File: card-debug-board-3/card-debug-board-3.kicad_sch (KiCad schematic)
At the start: 94 parts, among them J1 USB4105-GF-A, J2 USB4105-GF-A, J3 Conn_01x05, J4 5040501291, J5 2-1734592-0, Q1 PMV450ENEAR, SW1 B3F-1000, SW2 PCM13SMTR, SW3 B3F-1000, SW4 78RB02T, U1 MIC5205-3.3YM5, U2 W25Q16JVSS, U3 RP2040, U4 74AUP1G17, U5 74AUP1G17, U6 IP4234CZ6,125, U7 IP4234CZ6,125, Y1 12 MHz

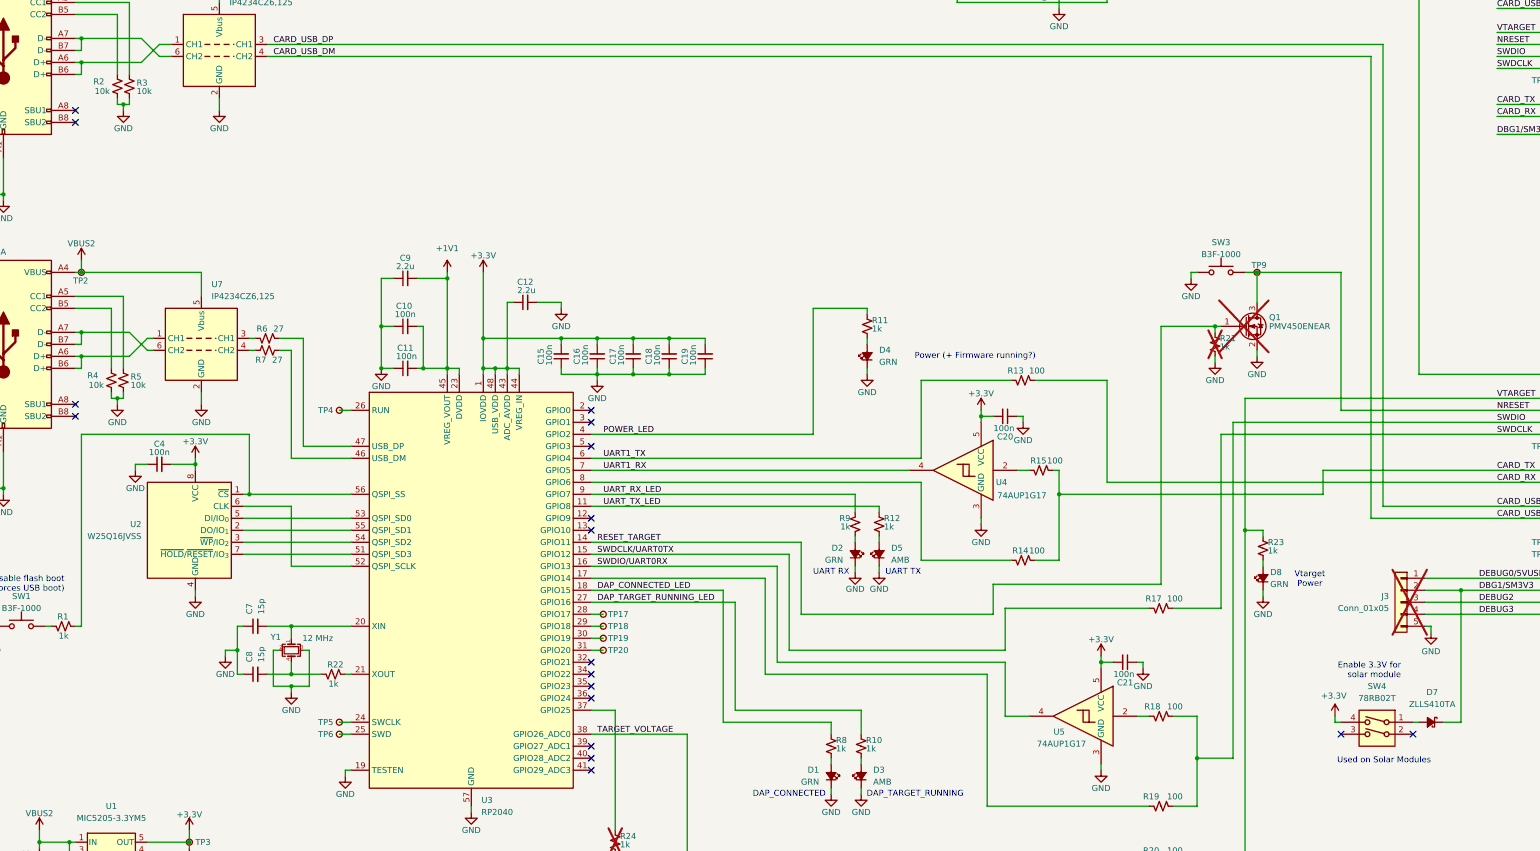
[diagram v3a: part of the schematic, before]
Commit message: Fix labeling of the 3.0 power slide switch which was exactly backwards.
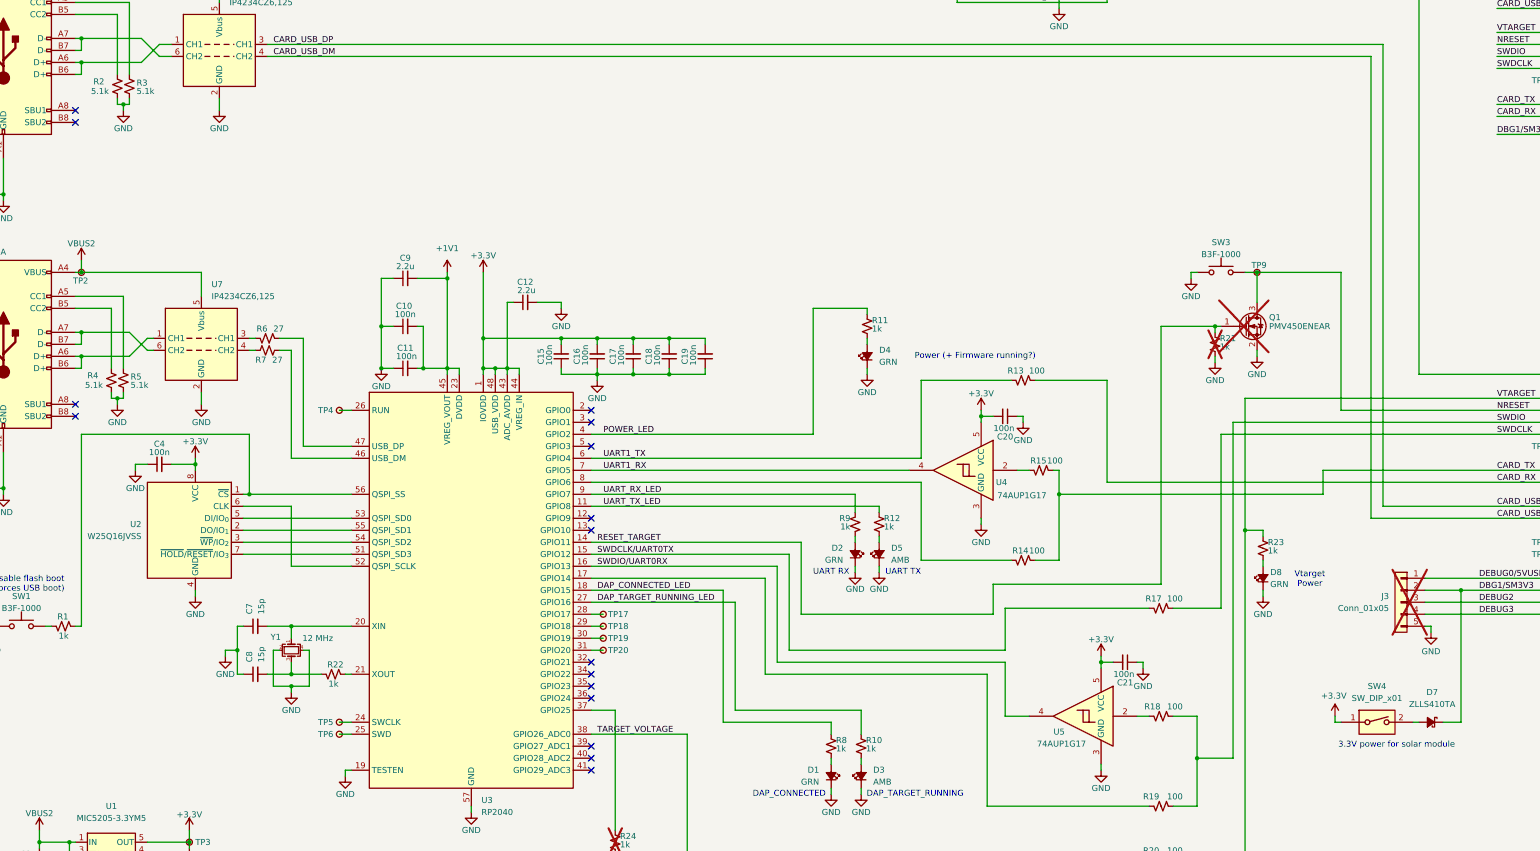
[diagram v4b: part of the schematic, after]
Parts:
- removed SW4: 78RB02T, Button_Switch_THT:SW_DIP_SPSTx02_Slide_6.7x6.64mm_W7.62mm_P2.54mm_LowProfile, symbol Switch:SW_DIP_x02
- added SW4: SW_DIP_x01, Button_Switch_THT:SW_DIP_SPSTx01_Slide_6.7x4.1mm_W7.62mm_P2.54mm_LowProfile, symbol Switch:SW_DIP_x01
- R2, R3, R4, R5: value 10k -> 5.1k; DPN RMCF0603FT10K0CT-ND -> RMCF0603FT5K10CT-ND; MPN RMCF0603FT10K0 -> RMCF0603FT5K10
- Y1: symbol Device:Crystal_GND23_Small -> Device:Crystal_GND24_Small
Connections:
- net +3.3V: now also SW4.1
- net GND: now also Y1.4; no longer Y1.3
- net at C8.2, R22.1: now also Y1.3; no longer Y1.4
- net at D7.2 (A): now also SW4.2
- no-connect marks 18 -> 16
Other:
- note added: "3.3V power for solar module"
- note removed: "Enable 3.3V for solar module"
- note removed: "Used on Solar Modules"
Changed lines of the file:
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@@
 	(title_block
 		(title "Card Debug Board")
-		(date "2025-11-10")
+		(date "2025-11-24")
 		(rev "3.1")
 		(company "Portland State Aerospace Society")
@@
 		)
 	)
-	(text "Enable 3.3V for\nsolar module"
+	(text "3.3V power for solar module"
 		(exclude_from_sim no)
-		(at 331.47 196.596 0)
+		(at 342.9 211.328 0)
 		(effects
 			(font
@@
 		)
 	)
-	(text "Used on Solar Modules"
-		(exclude_from_sim no)
-		(at 337.82 214.63 0)
-		(effects
-			(font
-				(size 1.27 1.27)
-			)
-			(justify right bottom)
-		)
-	)
 	(text "Heartbeat/Misc"
 		(exclude_from_sim no)
@@
 	)
 	(no_connect
-		(at 318.77 208.28)
-	)
-	(no_connect
 		(at 160.02 165.1)
 	)
@@
 	)
 	(no_connect
-		(at 334.01 208.28)
-	)
-	(no_connect
 		(at 160.02 142.24)
 	)
@@
 			)
 		)
-		(property "Value" "10k"
-			(at 54.864 72.136 0)
+		(property "Value" "5.1k"
+			(at 54.102 72.136 0)
 			(effects
 				(font
@@
 			)
 		)
-		(property "Description" "10 kOhms ±1% 0.1W, 1/10W Chip Resistor 0603 (1608 Metric) Automotive AEC-Q200 Thick Film"
+		(property "Description" "5.1 kOhms ±1% 0.1W, 1/10W Chip Resistor 0603 (1608 Metric) Automotive AEC-Q200 Thick Film"
 			(at 59.69 71.12 0)
 			(effects
@@
 			)
 		)
-		(property "DPN" "RMCF0603FT10K0CT-ND"
+		(property "DPN" "RMCF0603FT5K10CT-ND"
 			(at 59.69 71.12 0)
 			(effects
@@
 			)
 		)
-		(property "MPN" "RMCF0603FT10K0"
+		(property "MPN" "RMCF0603FT5K10"
 			(at 59.69 71.12 0)
 			(effects
@@
 			)
 		)
-		(property "Value" "10k"
+		(property "Value" "5.1k"
 			(at 62.484 134.366 0)
 			(effects
@@
 			)
 		)
-		(property "Description" "10 kOhms ±1% 0.1W, 1/10W Chip Resistor 0603 (1608 Metric) Automotive AEC-Q200 Thick Film"
+		(property "Description" "5.1 kOhms ±1% 0.1W, 1/10W Chip Resistor 0603 (1608 Metric) Automotive AEC-Q200 Thick Film"
 			(at 60.96 133.35 0)
 			(effects
@@
 			)
 		)
-		(property "DPN" "RMCF0603FT10K0CT-ND"
+		(property "DPN" "RMCF0603FT5K10CT-ND"
 			(at 60.96 133.35 0)
 			(effects
@@
 			)
 		)
-		(property "MPN" "RMCF0603FT10K0"
+		(property "MPN" "RMCF0603FT5K10"
 			(at 60.96 133.35 0)
 			(effects
@@
 	)
 	(symbol
-		(lib_id "Switch:SW_DIP_x02")
-		(at 326.39 208.28 0)
-		(mirror y)
-		(unit 1)
-		(exclude_from_sim no)
-		(in_bom yes)
-		(on_board yes)
-		(dnp no)
-		(fields_autoplaced yes)
-		(property "Reference" "SW4"
-			(at 326.39 198.12 0)
-			(effects
-				(font
-					(size 1.27 1.27)
-				)
-			)
-		)
-		(property "Value" "78RB02T"
-			(at 326.39 200.66 0)
-			(effects
-				(font
-					(size 1.27 1.27)
-				)
-			)
-		)
-		(property "Footprint" "Button_Switch_THT:SW_DIP_SPSTx02_Slide_6.7x6.64mm_W7.62mm_P2.54mm_LowProfile"
-			(at 326.39 208.28 0)
-			(effects
-				(font
-					(size 1.27 1.27)
-				)
-				(hide yes)
-			)
-		)
-		(property "Datasheet" "https://app-grayhill-website-cms-prod-001.azurewebsites.net/media/4nooheqb/78b-datasheet.pdf"
-			(at 326.39 208.28 0)
-			(effects
-				(font
-					(size 1.27 1.27)
-				)
-				(hide yes)
-			)
-		)
-		(property "Description" "Dip Switch SPST 2 Position Through Hole Slide (Standard) Actuator 150mA 30VDC"
-			(at 326.39 208.28 0)
-			(effects
-				(font
-					(size 1.27 1.27)
-				)
-				(hide yes)
-			)
-		)
-		(property "MFR" "Grayhill Inc."
-			(at 326.39 208.28 0)
-			(effects
-				(font
-					(size 1.27 1.27)
-				)
-				(hide yes)
-			)
-		)
-		(property "MPN" "78RB02T"
-			(at 326.39 208.28 0)
-			(effects
-				(font
-					(size 1.27 1.27)
-				)
-				(hide yes)
-			)
-		)
-		(property "DIS" "DigiKey"
-			(at 326.39 208.28 0)
-			(effects
-				(font
-					(size 1.27 1.27)
-				)
-				(hide yes)
-			)
-		)
-		(property "DPN" "GH7201-ND"
-			(at 326.39 208.28 0)
-			(effects
-				(font
-					(size 1.27 1.27)
-				)
-				(hide yes)
-			)
-		)
-		(pin "3"
-		)
-		(pin "1"
-		)
-		(pin "2"
-		)
-		(pin "4"
-		)
-		(instances
-			(project ""
-				(path "/6ec99451-f949-47af-a175-ad55f6cf8202"
-					(reference "SW4")
-					(unit 1)
-				)
-			)
-		)
-	)
-	(symbol
 		(lib_id "power:GND")
 		(at 218.44 132.08 0)
@@
 			)
 		)
-		(property "Value" "10k"
+		(property "Value" "5.1k"
 			(at 63.754 72.136 0)
 			(effects
@@
 			)
 		)
-		(property "Description" "10 kOhms ±1% 0.1W, 1/10W Chip Resistor 0603 (1608 Metric) Automotive AEC-Q200 Thick Film"
+		(property "Description" "5.1 kOhms ±1% 0.1W, 1/10W Chip Resistor 0603 (1608 Metric) Automotive AEC-Q200 Thick Film"
 			(at 62.23 71.12 0)
 			(effects
@@
 			)
 		)
-		(property "DPN" "RMCF0603FT10K0CT-ND"
+		(property "DPN" "RMCF0603FT5K10CT-ND"
 			(at 62.23 71.12 0)
 			(effects
@@
 			)
 		)
-		(property "MPN" "RMCF0603FT10K0"
+		(property "MPN" "RMCF0603FT5K10"
 			(at 62.23 71.12 0)
 			(effects
@@
 	)
 	(symbol
+		(lib_id "Switch:SW_DIP_x01")
+		(at 326.39 205.74 0)
+		(unit 1)
+		(exclude_from_sim no)
+		(in_bom yes)
+		(on_board yes)
+		(dnp no)
+		(fields_autoplaced yes)
+		(property "Reference" "SW4"
+			(at 326.39 198.12 0)
+			(effects
+				(font
+					(size 1.27 1.27)
+				)
+			)
+		)
+		(property "Value" "SW_DIP_x01"
+			(at 326.39 200.66 0)
+			(effects
+				(font
+					(size 1.27 1.27)
+				)
+			)
+		)
+		(property "Footprint" "Button_Switch_THT:SW_DIP_SPSTx01_Slide_6.7x4.1mm_W7.62mm_P2.54mm_LowProfile"
+			(at 326.39 205.74 0)
+			(effects
+				(font
+					(size 1.27 1.27)
+				)
+				(hide yes)
+			)
+		)
+		(property "Datasheet" "Dip Switch SPST 1 Position Through Hole Slide (Standard) Actuator 100mA 6VDC"
+			(at 326.39 205.74 0)
+			(effects
+				(font
+					(size 1.27 1.27)
+				)
+				(hide yes)
+			)
+		)
+		(property "Description" "1x DIP Switch, Single Pole Single Throw (SPST) switch, small symbol"
+			(at 326.39 205.74 0)
+			(effects
+				(font
+					(size 1.27 1.27)
+				)
+				(hide yes)
+			)
+		)
+		(property "MFR" "Nidec Components Corporation"
+			(at 326.39 205.74 0)
+			(effects
+				(font
+					(size 1.27 1.27)
+				)
+				(hide yes)
+			)
+		)
+		(property "MPN" "CFS-0100MC"
+			(at 326.39 205.74 0)
+			(effects
+				(font
+					(size 1.27 1.27)
+				)
+				(hide yes)
+			)
+		)
+		(property "DIS" "DigiKey"
+			(at 326.39 205.74 0)
+			(effects
+				(font
+					(size 1.27 1.27)
+				)
+				(hide yes)
+			)
+		)
+		(property "DPN" "563-2016-5-ND"
+			(at 326.39 205.74 0)
+			(effects
+				(font
+					(size 1.27 1.27)
+				)
+				(hide yes)
+			)
+		)
+		(pin "1"
+		)
+		(pin "2"
+		)
+		(instances
+			(project ""
+				(path "/6ec99451-f949-47af-a175-ad55f6cf8202"
+					(reference "SW4")
+					(unit 1)
+				)
+			)
+		)
+	)
+	(symbol
 		(lib_id "power:GND")
 		(at 367.03 189.23 0)
@@
 			)
 		)
-		(property "Value" "10k"
-			(at 53.594 134.366 0)
+		(property "Value" "5.1k"
+			(at 52.832 134.366 0)
 			(effects
 				(font
@@
 			)
 		)
-		(property "Description" "10 kOhms ±1% 0.1W, 1/10W Chip Resistor 0603 (1608 Metric) Automotive AEC-Q200 Thick Film"
+		(property "Description" "5.1 kOhms ±1% 0.1W, 1/10W Chip Resistor 0603 (1608 Metric) Automotive AEC-Q200 Thick Film"
 			(at 58.42 133.35 0)
 			(effects
@@
 			)
 		)
-		(property "DPN" "RMCF0603FT10K0CT-ND"
+		(property "DPN" "RMCF0603FT5K10CT-ND"
 			(at 58.42 133.35 0)
 			(effects
@@
 			)
 		)
-		(property "MPN" "RMCF0603FT10K0"
+		(property "MPN" "RMCF0603FT5K10"
 			(at 58.42 133.35 0)
 			(effects
@@
 	)
 	(symbol
-		(lib_id "Device:Crystal_GND23_Small")
+		(lib_id "Device:Crystal_GND24_Small")
 		(at 96.52 190.5 270)
 		(unit 1)
@@
 			)
 		)
-		(property "Datasheet" "https://www.raltron.com/webproducts/specs/CRYSTAL/RH100-12.000-12-1010-X-TR-NS2.pdf"
+		(property "Datasheet" "~"
 			(at 96.52 190.5 0)
 			(effects
@@
 			)
 		)
-		(property "Description" "12 MHz ±10ppm Crystal 12pF 50 Ohms 4-SMD, No Lead"
+		(property "Description" "Four pin crystal, GND on pins 2 and 4, small symbol"
 			(at 96.52 190.5 0)
 			(effects

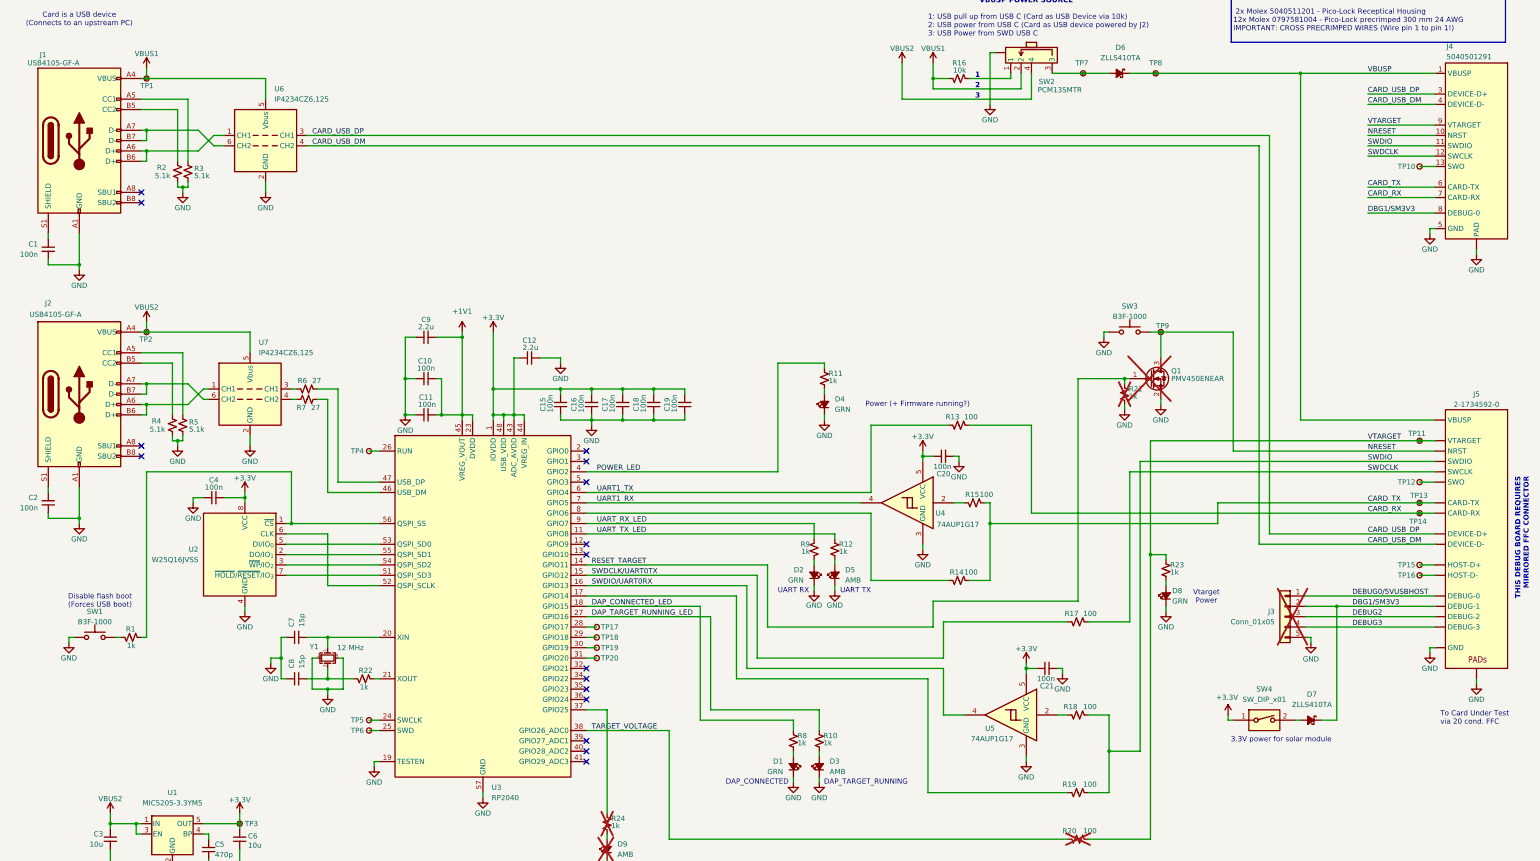
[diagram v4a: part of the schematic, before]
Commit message: Cleanup and last features.
Added ability for the RP2040 to power the DUT using a GPIO line. Cleaned up ERC and DRC. Updated symbols and footprints.
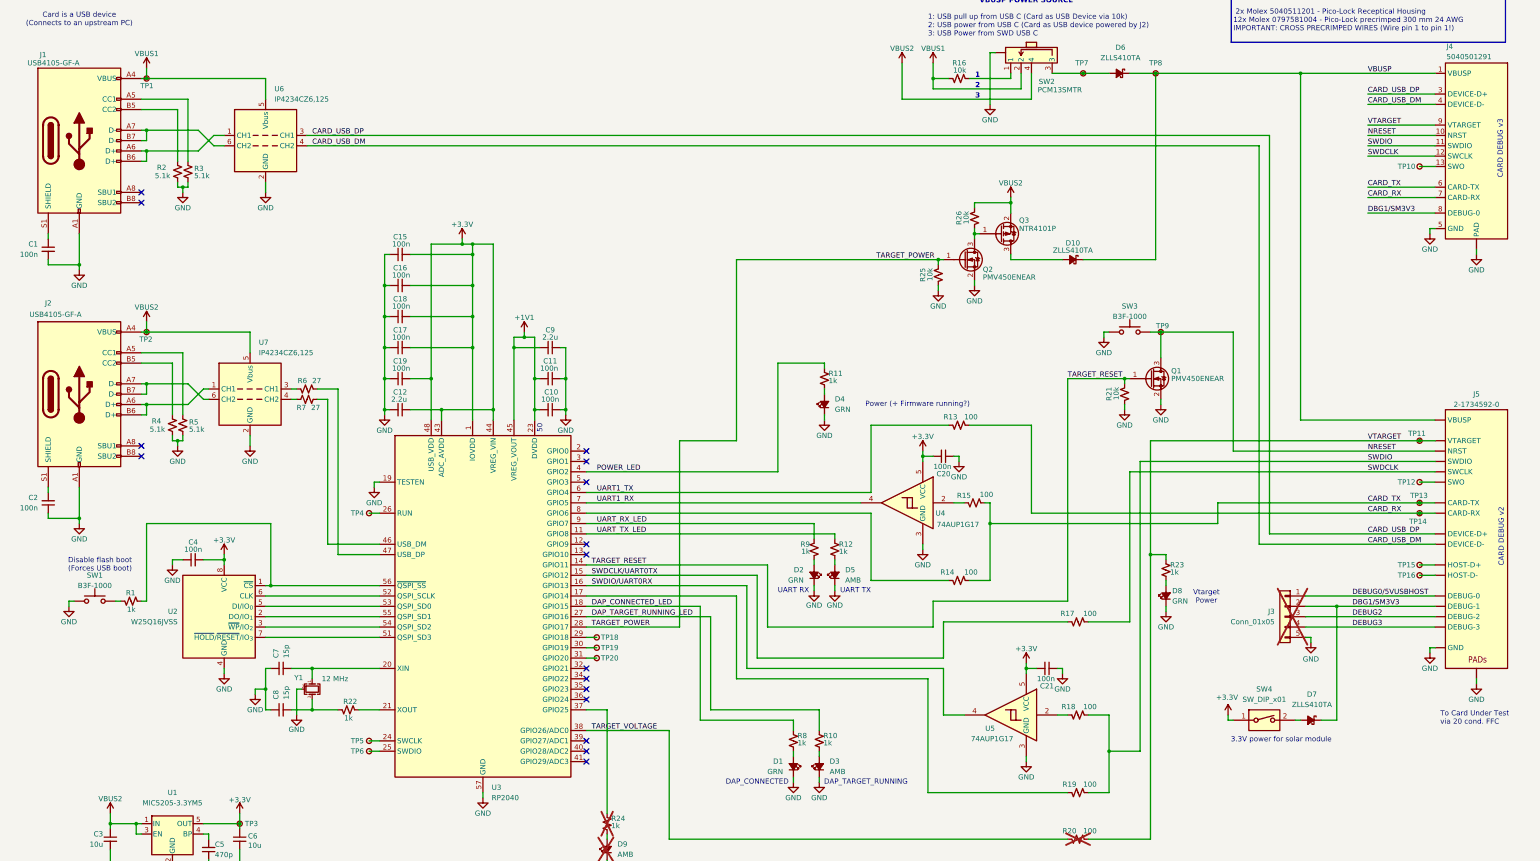
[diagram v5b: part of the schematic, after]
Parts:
- removed TP17: TestPoint-MinTH, oresat-misc:TestPoint-MinTH, symbol oresat-misc:TestPoint-MinTH
- added D10: ZLLS410TA, Diode_SMD:D_SOD-323, symbol Device:D_Schottky_Small_Filled
- added Q2: PMV450ENEAR, Package_TO_SOT_SMD:SOT-23, symbol Transistor_FET_Other:Q_NMOS_Depletion_GSD
- added Q3: NTR4101P, Package_TO_SOT_SMD:SOT-23, symbol Transistor_FET:NTR2101P
- added R25, R26: 10k, oresat-passives:0603-C-NOSILK, symbol Device:R_Small_US
- J5: symbol oresat-connectors:J-TE-Debug-2-1734592-0 -> oresat-connectors:J-TE-2-1734592-0
- Q1: now fitted
- R21: value 1k -> 10k; DIS (none) -> DigiKey; DPN (none) -> RMCF0603FT10K0CT-ND; MFR (none) -> Stackpole Electronics Inc; MPN (none) -> RMCF0603FT10K0; now fitted
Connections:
- net GND: now also Q2.2 (S), R25.1
- net VBUS2: now also Q3.2 (S), R26.2
- net VBUSP: now also D10.1 (K)
- net TARGET_POWER: now reaches U3.28 (GPIO17)
- net TARGET_POWER: now also Q2.1 (G), R25.2
- net RESET_TARGET renamed TARGET_RESET
- new net: Q2.3 (D), Q3.1 (G), R26.1
- new net: D10.2 (A), Q3.3 (D)
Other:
- note added: "50"
- note added: "CARD DEBUG v2"
- note added: "CARD DEBUG v3"
- note removed: "THIS DEBUG BOARD REQUIRES MIRRORED FFC CONNECTOR"
- moved on the sheet: C10, C11, C12, C15, C16, C17, C18, C19, C4, C7, C8, C9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

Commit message: BOM cleanup; fabbing v3.1git add .
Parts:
- C1, C10, C11, C15, C16, C17, C18, C19, C2, C20, C21, C4: DPN 587-3472-1-ND -> 399-6856-1-ND; MFR Taiyo Yuden -> KEMET; MPN TMK107BJ104KAHT -> C0603C104K5RACAUTO
- C12, C9: DPN 587-4929-1-ND -> 490-GRT188C71E225KE13DCT-ND; MFR Taiyo Yuden -> Murata Electronics; MPN TMK107BBJ225MAHT -> GRT188C71E225KE13D
- C3, C6: DIS DIgiKey -> DigiKey; DPN 490-GRT21BC71E106KE13LCT-ND -> 490-GRT21BC71E106KE13KCT-ND; MPN GRT21BC71E106KE13L -> GRT21BC71E106KE13K
- C5: DPN 1276-6700-1-ND -> 399-6894-1-ND; MFR Samsung -> KEMET; MPN CL10B471KC8WPNC -> C0603C471K5RACAUTO
- Q3: DIS (none) -> DigiKey; DPN (none) -> NTR4101PT1GOSCT-ND; MFR (none) -> ON Semi; MPN (none) -> NTR4101PT1G
